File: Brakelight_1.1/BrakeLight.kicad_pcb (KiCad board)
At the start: 2 copper layers, 99 x 20 mm, 39 parts, among them J1 Conn_01x02_Female, U1 LM317MABDTG

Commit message: Adapted to PM09
Changing the power footprint and changing several tracks
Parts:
- removed J1: Conn_01x02_Female, footprint:LEMO EEG00302CLL
- added J2: Conn_01x01_Socket, Connector_Wire:SolderWire-0.75sqmm_1x01_D1.25mm_OD3.5mm, F.Cu at (102.0, 150.1)
- added J3: Conn_01x01_Socket, Connector_Wire:SolderWire-0.75sqmm_1x01_D1.25mm_OD3.5mm, F.Cu at (109.0, 150.2)
- moved D1 3.30 mm to (105.7, 154.2)
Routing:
- net +24V: track 30.7 -> 21.1 mm, vias 8 -> 9
- net SIG_BRAKE: track 120.1 -> 120.9 mm, vias 10 -> 12
- net /ADJ: track 109.1 -> 108.9 mm, vias 6 -> 2
- net chłodzenie(Vout): vias 19 -> 11
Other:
- outline, holes or cut-outs redrawn

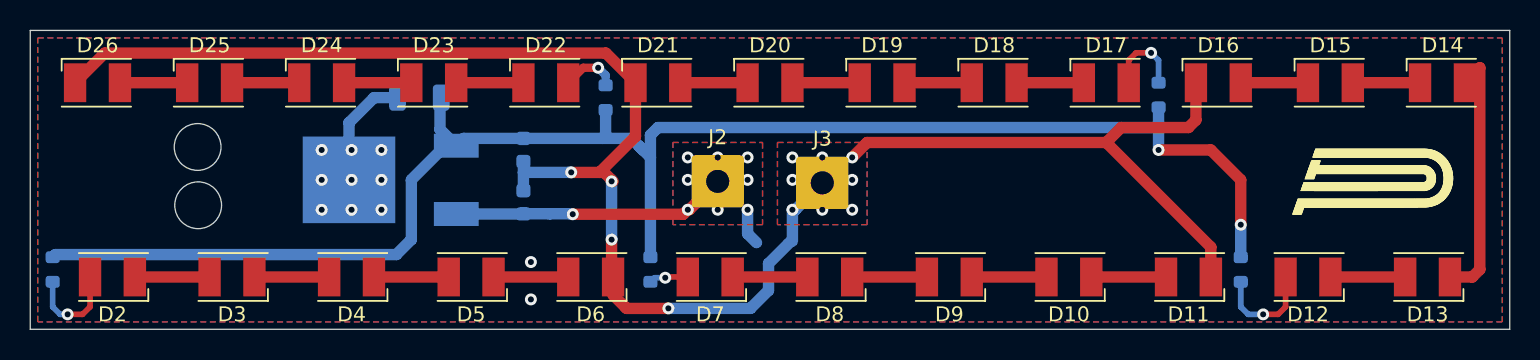
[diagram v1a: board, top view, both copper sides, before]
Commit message: Changing the housing of the LED section resistors to larger ones 0603 -> 1206
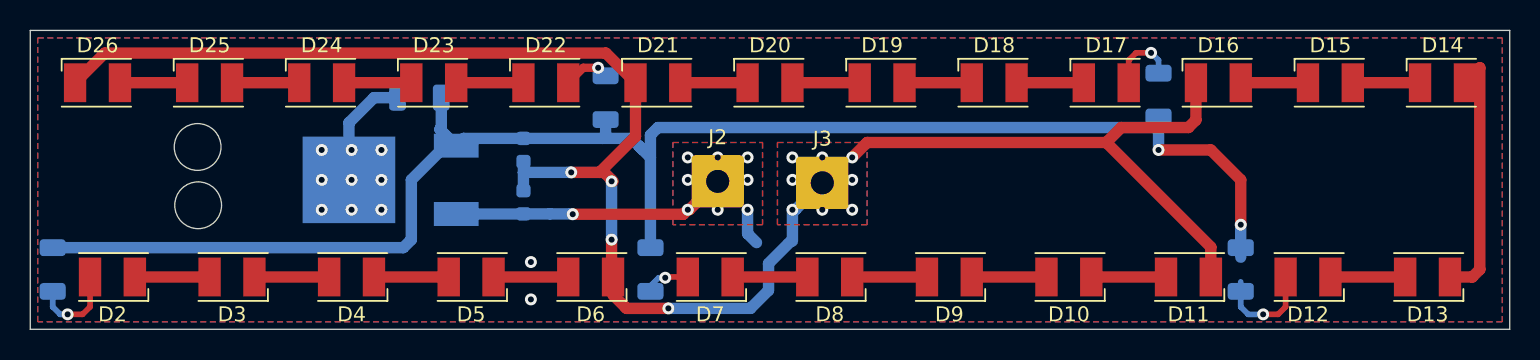
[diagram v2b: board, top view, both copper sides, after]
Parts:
- removed G*** (x3): LOGO, Logos:PUTM_LOGO_13mm
- R1, R3, R4, R5, R6: footprint Resistor_SMD:R_0603_1608Metric -> Resistor_SMD:R_1206_3216Metric
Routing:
- net /ADJ: track 108.9 -> 106.8 mm
- net Net-(D22-A): track 3.80 -> 3.16 mm
- net Net-(D2-A): track 6.59 -> 5.95 mm
- net Net-(D17-A): track 5.41 -> 4.78 mm
